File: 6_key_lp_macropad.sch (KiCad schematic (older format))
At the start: 15 parts, among them SW1 Rotary_Encoder_Switch, SW2 SW_Push, U1 ProMicro

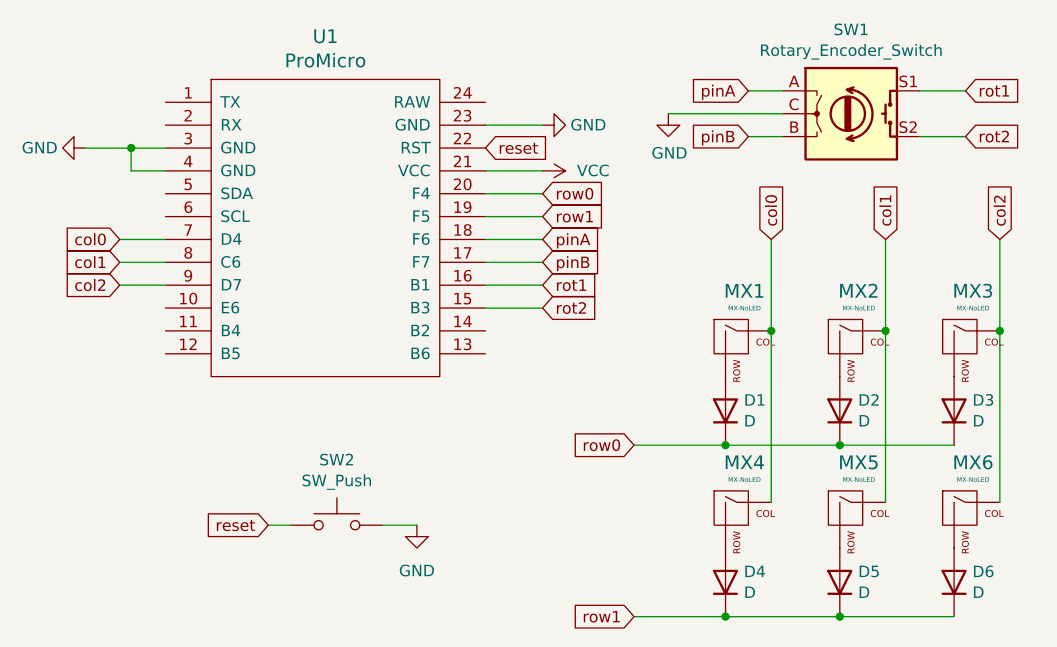
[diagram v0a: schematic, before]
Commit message: Changed to Direct Pin assignment
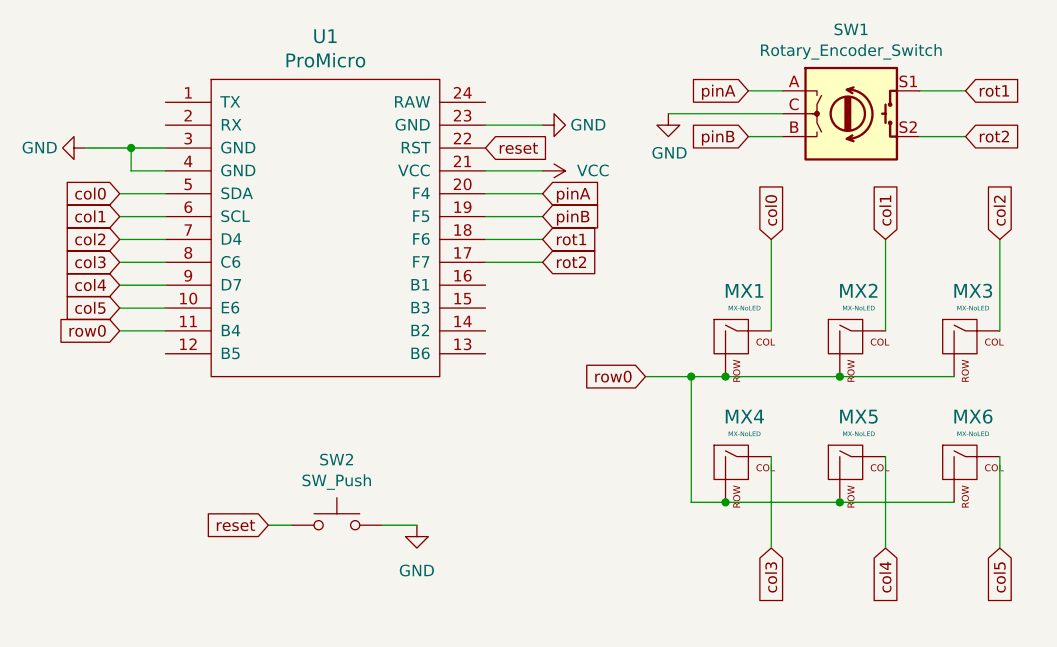
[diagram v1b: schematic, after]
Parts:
- removed D1, D2, D3, D4, D5, D6: D, symbol Device:D
- MX1, MX2, MX3, MX4, MX5, MX6: footprint (none) -> Kailh_Choc:KailhChoc-1U
- SW1: footprint (none) -> Rotary_Encoder:RotaryEncoder_Alps_EC11E-Switch_Vertical_H20mm
- SW2: footprint (none) -> random-keyboard-parts:SKQG-1155865
- U1: footprint (none) -> promicro:ProMicro
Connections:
- net row1 is gone; now on net pinB: U1.19 (F5)
- net col0: now also U1.5 (SDA); no longer MX4.1 (COL), U1.7 (D4)
- net col1: now also U1.6 (SCL); no longer MX5.1 (COL), U1.8 (C6)
- net col2: now also U1.7 (D4); no longer MX6.1 (COL), U1.9 (D7)
- net pinA: now also U1.20 (F4); no longer U1.18 (F6)
- net pinB: no longer U1.17 (F7)
- net rot1: now also U1.18 (F6); no longer U1.16 (B1)
- net rot2: now also U1.17 (F7); no longer U1.15 (B3)
- net row0: now also MX1.2 (ROW), MX2.2 (ROW), MX3.2 (ROW), MX4.2 (ROW), MX5.2 (ROW), MX6.2 (ROW), U1.11 (B4); no longer U1.20 (F4)
- net col5: now reaches U1.10 (E6)
- net col5: now also MX6.1 (COL)
- new net col3: MX4.1 (COL), U1.8 (C6)
- new net col4: MX5.1 (COL), U1.9 (D7)
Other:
- moved on the sheet: MX4, MX5, MX6
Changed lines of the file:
@@
 F 0 "U1" H 4900 4787 60  0000 C CNN
 F 1 "ProMicro" H 4900 4681 60  0000 C CNN
-F 2 "" H 5000 2700 60  0000 C CNN
+F 2 "promicro:ProMicro" H 5000 2700 60  0001 C CNN
 F 3 "" H 5000 2700 60  0000 C CNN
 	1    4900 3750
@@
 F 0 "SW1" H 7200 3417 50  0000 C CNN
 F 1 "Rotary_Encoder_Switch" H 7200 3326 50  0000 C CNN
-F 2 "" H 7050 3210 50  0001 C CNN
+F 2 "Rotary_Encoder:RotaryEncoder_Alps_EC11E-Switch_Vertical_H20mm" H 7050 3210 50  0001 C CNN
 F 3 "~" H 7200 3310 50  0001 C CNN
 	1    7200 3050
@@
 Wire Wire Line
 	5600 3300 5850 3300
+Text GLabel 4000 3400 0    50   Input ~ 0
+col0
+Wire Wire Line
+	4200 3400 4000 3400
+Text GLabel 4000 3500 0    50   Input ~ 0
+col1
+Wire Wire Line
+	4200 3500 4000 3500
 Text GLabel 4000 3600 0    50   Input ~ 0
-col0
+col2
 Wire Wire Line
 	4200 3600 4000 3600
-Text GLabel 4000 3700 0    50   Input ~ 0
-col1
-Wire Wire Line
-	4200 3700 4000 3700
-Text GLabel 4000 3800 0    50   Input ~ 0
-col2
-Wire Wire Line
-	4200 3800 4000 3800
 $Comp
 L power:GND #PWR0104
@@
 F 0 "MX1" H 6733 4273 60  0000 C CNN
 F 1 "MX-NoLED" H 6733 4199 20  0000 C CNN
-F 2 "" H 6075 4025 60  0001 C CNN
+F 2 "Kailh_Choc:KailhChoc-1U" H 6075 4025 60  0001 C CNN
 F 3 "" H 6075 4025 60  0001 C CNN
 	1    6700 4050
@@
 F 0 "MX2" H 7233 4273 60  0000 C CNN
 F 1 "MX-NoLED" H 7233 4199 20  0000 C CNN
-F 2 "" H 6575 4025 60  0001 C CNN
+F 2 "Kailh_Choc:KailhChoc-1U" H 6575 4025 60  0001 C CNN
 F 3 "" H 6575 4025 60  0001 C CNN
 	1    7200 4050
@@
 F 0 "MX3" H 7733 4273 60  0000 C CNN
 F 1 "MX-NoLED" H 7733 4199 20  0000 C CNN
-F 2 "" H 7075 4025 60  0001 C CNN
+F 2 "Kailh_Choc:KailhChoc-1U" H 7075 4025 60  0001 C CNN
 F 3 "" H 7075 4025 60  0001 C CNN
 	1    7700 4050
@@
 L MX_Alps_Hybrid:MX-NoLED MX6
 U 1 1 62CCE05A
-P 7700 4800
-F 0 "MX6" H 7733 5023 60  0000 C CNN
-F 1 "MX-NoLED" H 7733 4949 20  0000 C CNN
-F 2 "" H 7075 4775 60  0001 C CNN
-F 3 "" H 7075 4775 60  0001 C CNN
-	1    7700 4800
+P 7700 4600
+F 0 "MX6" H 7733 4823 60  0000 C CNN
+F 1 "MX-NoLED" H 7733 4749 20  0000 C CNN
+F 2 "Kailh_Choc:KailhChoc-1U" H 7075 4575 60  0001 C CNN
+F 3 "" H 7075 4575 60  0001 C CNN
+	1    7700 4600
 	1    0    0    -1
 $EndComp
@@
 L MX_Alps_Hybrid:MX-NoLED MX5
 U 1 1 62CCE444
-P 7200 4800
-F 0 "MX5" H 7233 5023 60  0000 C CNN
-F 1 "MX-NoLED" H 7233 4949 20  0000 C CNN
-F 2 "" H 6575 4775 60  0001 C CNN
-F 3 "" H 6575 4775 60  0001 C CNN
-	1    7200 4800
+P 7200 4600
+F 0 "MX5" H 7233 4823 60  0000 C CNN
+F 1 "MX-NoLED" H 7233 4749 20  0000 C CNN
+F 2 "Kailh_Choc:KailhChoc-1U" H 6575 4575 60  0001 C CNN
+F 3 "" H 6575 4575 60  0001 C CNN
+	1    7200 4600
 	1    0    0    -1
 $EndComp
@@
 L MX_Alps_Hybrid:MX-NoLED MX4
 U 1 1 62CCEA2C
-P 6700 4800
-F 0 "MX4" H 6733 5023 60  0000 C CNN
-F 1 "MX-NoLED" H 6733 4949 20  0000 C CNN
-F 2 "" H 6075 4775 60  0001 C CNN
-F 3 "" H 6075 4775 60  0001 C CNN
-	1    6700 4800
-	1    0    0    -1
-$EndComp
-Text GLabel 5850 3900 2    50   Input ~ 0
+P 6700 4600
+F 0 "MX4" H 6733 4823 60  0000 C CNN
+F 1 "MX-NoLED" H 6733 4749 20  0000 C CNN
+F 2 "Kailh_Choc:KailhChoc-1U" H 6075 4575 60  0001 C CNN
+F 3 "" H 6075 4575 60  0001 C CNN
+	1    6700 4600
+	1    0    0    -1
+$EndComp
+Text GLabel 5850 3700 2    50   Input ~ 0
 rot2
-Text GLabel 5850 3800 2    50   Input ~ 0
+Text GLabel 5850 3600 2    50   Input ~ 0
 rot1
-Text GLabel 5850 3700 2    50   Input ~ 0
+Text GLabel 5850 3500 2    50   Input ~ 0
 pinB
-Text GLabel 5850 3600 2    50   Input ~ 0
+Text GLabel 5850 3400 2    50   Input ~ 0
 pinA
-Text GLabel 5850 3500 2    50   Input ~ 0
-row1
-Text GLabel 5850 3400 2    50   Input ~ 0
+Text GLabel 4000 4000 0    50   Input ~ 0
 row0
 Wire Wire Line
@@
 Wire Wire Line
 	5600 3700 5850 3700
-Wire Wire Line
-	5600 3800 5850 3800
-Wire Wire Line
-	5600 3900 5850 3900
 Text GLabel 7700 2950 2    50   Input ~ 0
 rot1
@@
 Wire Wire Line
 	7850 3600 7850 4000
-Text GLabel 6250 4500 0    50   Input ~ 0
+Text GLabel 6300 4200 0    50   Input ~ 0
 row0
-Text GLabel 6250 5250 0    50   Input ~ 0
-row1
-Wire Wire Line
-	7850 4000 7850 4750
-Wire Wire Line
-	7350 4000 7350 4750
-Wire Wire Line
-	6850 4000 6850 4750
-$Comp
-L Device:D D1
-U 1 1 62CE7421
-P 6650 4350
-F 0 "D1" V 6696 4270 50  0000 R CNN
-F 1 "D" V 6605 4270 50  0000 R CNN
-F 2 "" H 6650 4350 50  0001 C CNN
-F 3 "~" H 6650 4350 50  0001 C CNN
-	1    6650 4350
-	0    -1   -1   0
-$EndComp
-$Comp
-L Device:D D2
-U 1 1 62CEBAD1
-P 7150 4350
-F 0 "D2" V 7196 4270 50  0000 R CNN
-F 1 "D" V 7105 4270 50  0000 R CNN
-F 2 "" H 7150 4350 50  0001 C CNN
-F 3 "~" H 7150 4350 50  0001 C CNN
-	1    7150 4350
-	0    -1   -1   0
-$EndComp
-$Comp
-L Device:D D3
-U 1 1 62CEBF48
-P 7650 4350
-F 0 "D3" V 7696 4270 50  0000 R CNN
-F 1 "D" V 7605 4270 50  0000 R CNN
-F 2 "" H 7650 4350 50  0001 C CNN
-F 3 "~" H 7650 4350 50  0001 C CNN
-	1    7650 4350
-	0    -1   -1   0
-$EndComp
-Wire Wire Line
-	6650 4500 7150 4500
-Connection ~ 7150 4500
-Wire Wire Line
-	7150 4500 7650 4500
-Connection ~ 6850 4000
-Connection ~ 7350 4000
-Connection ~ 7850 4000
-$Comp
-L Device:D D4
-U 1 1 62CEFF8A
-P 6650 5100
-F 0 "D4" V 6696 5020 50  0000 R CNN
-F 1 "D" V 6605 5020 50  0000 R CNN
-F 2 "" H 6650 5100 50  0001 C CNN
-F 3 "~" H 6650 5100 50  0001 C CNN
-	1    6650 5100
-	0    -1   -1   0
-$EndComp
-$Comp
-L Device:D D5
-U 1 1 62CF0730
-P 7150 5100
-F 0 "D5" V 7196 5020 50  0000 R CNN
-F 1 "D" V 7105 5020 50  0000 R CNN
-F 2 "" H 7150 5100 50  0001 C CNN
-F 3 "~" H 7150 5100 50  0001 C CNN
-	1    7150 5100
-	0    -1   -1   0
-$EndComp
-$Comp
-L Device:D D6
-U 1 1 62CF0D5A
-P 7650 5100
-F 0 "D6" V 7696 5020 50  0000 R CNN
-F 1 "D" V 7605 5020 50  0000 R CNN
-F 2 "" H 7650 5100 50  0001 C CNN
-F 3 "~" H 7650 5100 50  0001 C CNN
-	1    7650 5100
-	0    -1   -1   0
-$EndComp
-Wire Wire Line
-	6650 5250 7150 5250
-Connection ~ 7150 5250
-Wire Wire Line
-	7150 5250 7650 5250
-Wire Wire Line
-	6650 4500 6250 4500
-Connection ~ 6650 4500
-Wire Wire Line
-	6650 5250 6250 5250
-Connection ~ 6650 5250
 Text GLabel 4650 4850 0    50   Input ~ 0
 reset
@@
 F 0 "SW2" H 4950 5135 50  0000 C CNN
 F 1 "SW_Push" H 4950 5044 50  0000 C CNN
-F 2 "" H 4950 5050 50  0001 C CNN
+F 2 "random-keyboard-parts:SKQG-1155865" H 4950 5050 50  0001 C CNN
 F 3 "~" H 4950 5050 50  0001 C CNN
 	1    4950 4850
@@
 Wire Wire Line
 	4650 4850 4750 4850
+Text GLabel 4000 3700 0    50   Input ~ 0
+col3
+Text GLabel 4000 3800 0    50   Input ~ 0
+col4
+Text GLabel 4000 3900 0    50   Input ~ 0
+col5
+Wire Wire Line
+	6300 4200 6500 4200
+Connection ~ 6650 4200
+Wire Wire Line
+	6650 4200 7150 4200
+Connection ~ 7150 4200
+Wire Wire Line
+	7150 4200 7650 4200
+Wire Wire Line
+	6500 4200 6500 4750
+Wire Wire Line
+	6500 4750 6650 4750
+Connection ~ 6500 4200
+Wire Wire Line
+	6500 4200 6650 4200
+Connection ~ 6650 4750
+Wire Wire Line
+	6650 4750 7150 4750
+Connection ~ 7150 4750
+Wire Wire Line
+	7150 4750 7650 4750
+Text GLabel 7350 4950 3    50   Input ~ 0
+col4
+Text GLabel 7850 4950 3    50   Input ~ 0
+col5
+Text GLabel 6850 4950 3    50   Input ~ 0
+col3
+Wire Wire Line
+	4000 3700 4200 3700
+Wire Wire Line
+	4200 3800 4000 3800
+Wire Wire Line
+	4200 3900 4000 3900
+Wire Wire Line
+	4000 4000 4200 4000
+Wire Wire Line
+	7850 4950 7850 4550
+Wire Wire Line
+	7350 4950 7350 4550
+Wire Wire Line
+	6850 4950 6850 4550
 $EndSCHEMATC

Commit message: Made the first PCB version
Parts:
- U1: footprint promicro:ProMicro -> promicro:ProMicro-NoSilk
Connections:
- net col0: now also U1.6 (SCL); no longer U1.5 (SDA)
- net col1: now also U1.7 (D4); no longer U1.6 (SCL)
- net col2: now also U1.9 (D7); no longer U1.7 (D4)
- net col4: now also U1.11 (B4); no longer U1.9 (D7)
- net pinA: now also U1.19 (F5); no longer U1.20 (F4)
- net pinB: now also U1.20 (F4); no longer U1.19 (F5)
- net row0: now also U1.5 (SDA); no longer U1.11 (B4)
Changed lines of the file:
@@
 F 0 "U1" H 4900 4787 60  0000 C CNN
 F 1 "ProMicro" H 4900 4681 60  0000 C CNN
-F 2 "promicro:ProMicro" H 5000 2700 60  0001 C CNN
+F 2 "promicro:ProMicro-NoSilk" H 5000 2700 60  0001 C CNN
 F 3 "" H 5000 2700 60  0000 C CNN
 	1    4900 3750
@@
 Wire Wire Line
 	5600 3300 5850 3300
-Text GLabel 4000 3400 0    50   Input ~ 0
-col0
 Wire Wire Line
 	4200 3400 4000 3400
-Text GLabel 4000 3500 0    50   Input ~ 0
-col1
 Wire Wire Line
 	4200 3500 4000 3500
-Text GLabel 4000 3600 0    50   Input ~ 0
-col2
 Wire Wire Line
 	4200 3600 4000 3600
@@
 Text GLabel 5850 3600 2    50   Input ~ 0
 rot1
+Text GLabel 5850 3400 2    50   Input ~ 0
+pinB
 Text GLabel 5850 3500 2    50   Input ~ 0
-pinB
-Text GLabel 5850 3400 2    50   Input ~ 0
 pinA
-Text GLabel 4000 4000 0    50   Input ~ 0
-row0
 Wire Wire Line
 	5600 3400 5850 3400
@@
 Wire Wire Line
 	4650 4850 4750 4850
-Text GLabel 4000 3700 0    50   Input ~ 0
-col3
-Text GLabel 4000 3800 0    50   Input ~ 0
+Text GLabel 4000 4000 0    50   Input ~ 0
 col4
 Text GLabel 4000 3900 0    50   Input ~ 0
@@
 Wire Wire Line
 	6850 4950 6850 4550
+Text GLabel 4000 3400 0    50   Input ~ 0
+row0
+Text GLabel 4000 3700 0    50   Input ~ 0
+col3
+Text GLabel 4000 3800 0    50   Input ~ 0
+col2
+Text GLabel 4000 3600 0    50   Input ~ 0
+col1
+Text GLabel 4000 3500 0    50   Input ~ 0
+col0
 $EndSCHEMATC

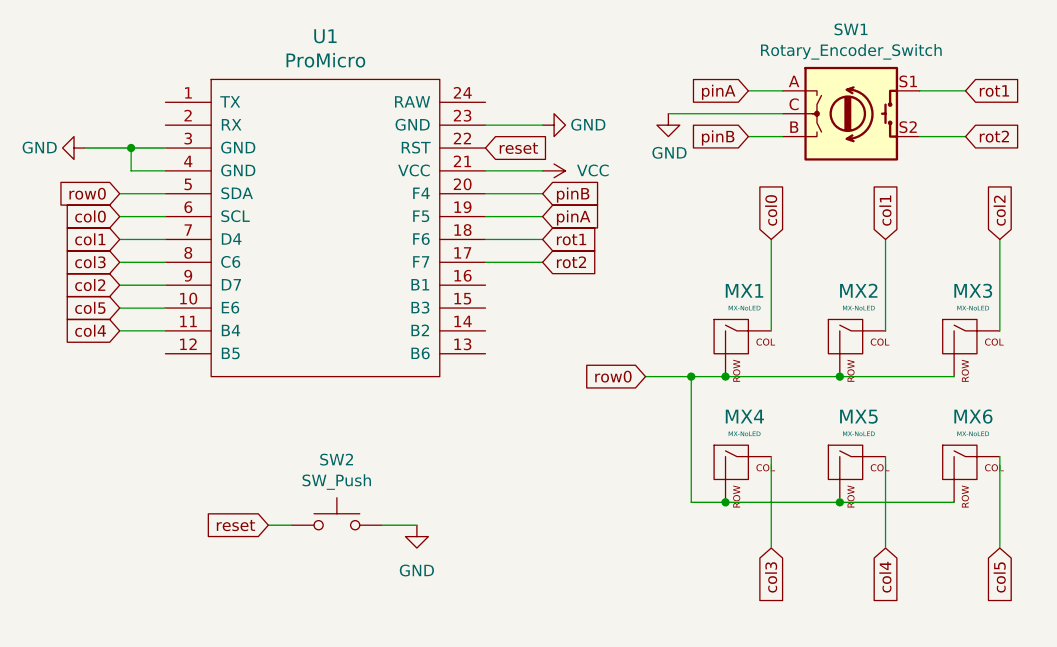
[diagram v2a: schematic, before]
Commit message: Flipped MCU to allow for stronger USB connector
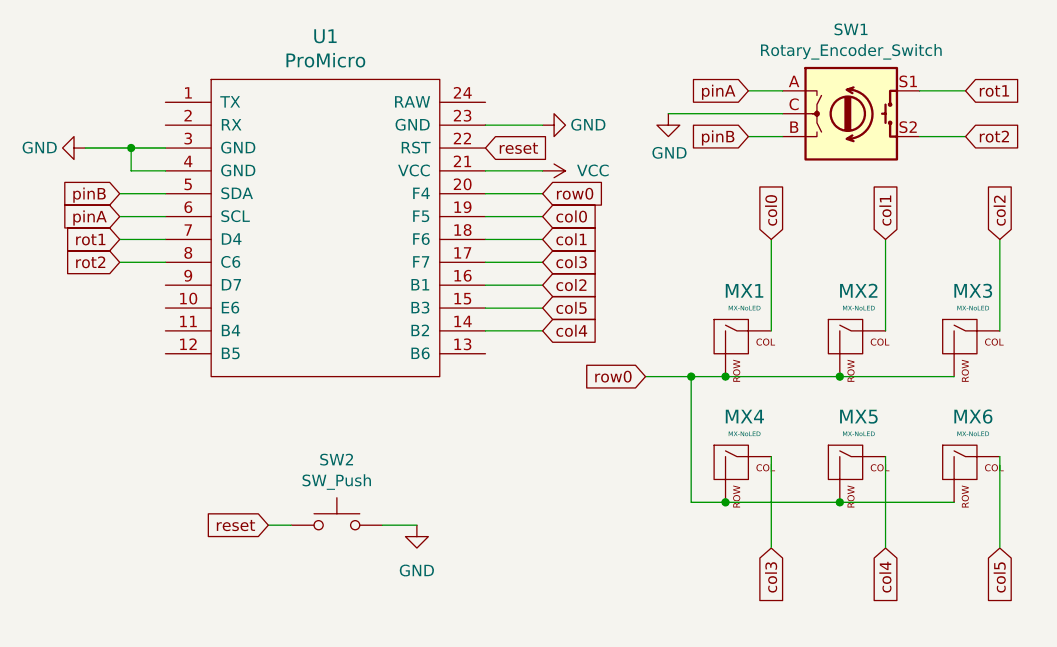
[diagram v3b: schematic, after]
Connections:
- net col0: now also U1.19 (F5); no longer U1.6 (SCL)
- net col1: now also U1.18 (F6); no longer U1.7 (D4)
- net col2: now also U1.16 (B1); no longer U1.9 (D7)
- net col3: now also U1.17 (F7); no longer U1.8 (C6)
- net col4: now also U1.14 (B2); no longer U1.11 (B4)
- net col5: now also U1.15 (B3); no longer U1.10 (E6)
- net pinA: now also U1.6 (SCL); no longer U1.19 (F5)
- net pinB: now also U1.5 (SDA); no longer U1.20 (F4)
- net rot1: now also U1.7 (D4); no longer U1.18 (F6)
- net rot2: now also U1.8 (C6); no longer U1.17 (F7)
- net row0: now also U1.20 (F4); no longer U1.5 (SDA)
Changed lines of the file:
@@
 	1    0    0    -1
 $EndComp
-Text GLabel 5850 3700 2    50   Input ~ 0
+Text GLabel 4000 3700 0    50   Input ~ 0
 rot2
-Text GLabel 5850 3600 2    50   Input ~ 0
-rot1
-Text GLabel 5850 3400 2    50   Input ~ 0
+Text GLabel 4000 3400 0    50   Input ~ 0
 pinB
-Text GLabel 5850 3500 2    50   Input ~ 0
+Text GLabel 4000 3500 0    50   Input ~ 0
 pinA
 Wire Wire Line
@@
 Wire Wire Line
 	4650 4850 4750 4850
-Text GLabel 4000 4000 0    50   Input ~ 0
+Text GLabel 5850 4000 2    50   Input ~ 0
 col4
-Text GLabel 4000 3900 0    50   Input ~ 0
+Text GLabel 5850 3900 2    50   Input ~ 0
 col5
 Wire Wire Line
@@
 	4000 3700 4200 3700
 Wire Wire Line
-	4200 3800 4000 3800
-Wire Wire Line
-	4200 3900 4000 3900
-Wire Wire Line
-	4000 4000 4200 4000
-Wire Wire Line
 	7850 4950 7850 4550
 Wire Wire Line
@@
 Wire Wire Line
 	6850 4950 6850 4550
-Text GLabel 4000 3400 0    50   Input ~ 0
+Text GLabel 5850 3400 2    50   Input ~ 0
 row0
-Text GLabel 4000 3700 0    50   Input ~ 0
+Text GLabel 5850 3700 2    50   Input ~ 0
 col3
-Text GLabel 4000 3800 0    50   Input ~ 0
+Text GLabel 5850 3800 2    50   Input ~ 0
 col2
+Text GLabel 5850 3600 2    50   Input ~ 0
+col1
+Text GLabel 5850 3500 2    50   Input ~ 0
+col0
 Text GLabel 4000 3600 0    50   Input ~ 0
-col1
-Text GLabel 4000 3500 0    50   Input ~ 0
-col0
+rot1
+Wire Wire Line
+	5600 3800 5850 3800
+Wire Wire Line
+	5600 3900 5850 3900
+Wire Wire Line
+	5600 4000 5850 4000
 $EndSCHEMATC

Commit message: Corrected for direct pin assignment
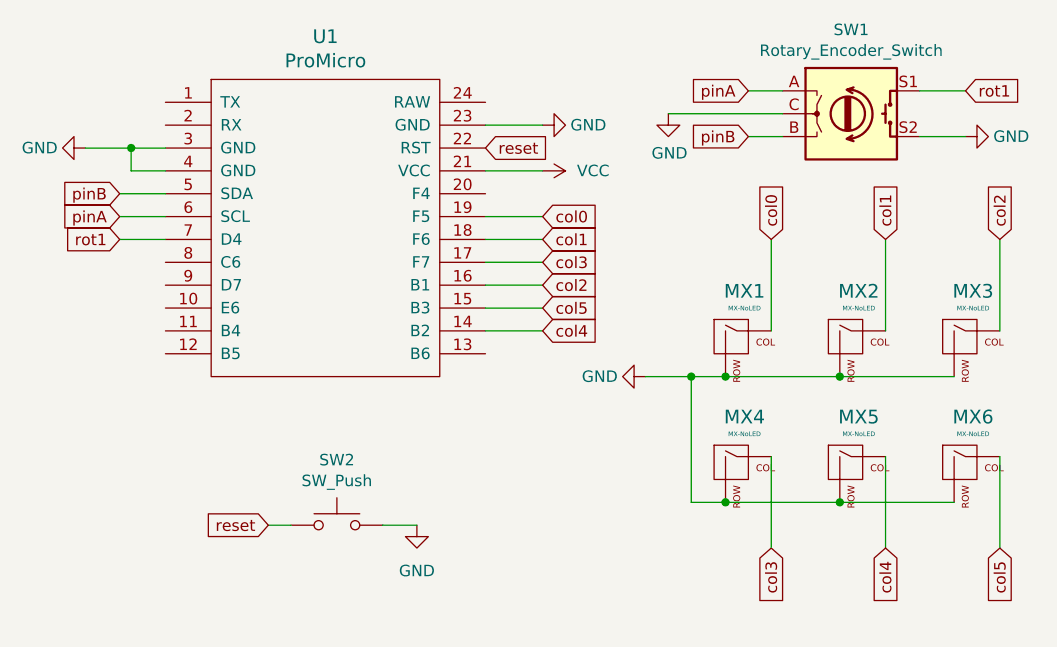
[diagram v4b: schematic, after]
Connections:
- net GND: now also MX1.2 (ROW), MX2.2 (ROW), MX3.2 (ROW), MX4.2 (ROW), MX5.2 (ROW), MX6.2 (ROW), SW1.S2
- net rot2: no longer names the net of U1.8 (C6)
- net rot2: no longer SW1.S2
- removed net row0: MX1.2 (ROW), MX2.2 (ROW), MX3.2 (ROW), MX4.2 (ROW), MX5.2 (ROW), MX6.2 (ROW), U1.20 (F4)
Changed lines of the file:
@@
 	1    0    0    -1
 $EndComp
-Text GLabel 4000 3700 0    50   Input ~ 0
-rot2
 Text GLabel 4000 3400 0    50   Input ~ 0
 pinB
 Text GLabel 4000 3500 0    50   Input ~ 0
 pinA
-Wire Wire Line
-	5600 3400 5850 3400
 Wire Wire Line
 	5600 3500 5850 3500
@@
 Text GLabel 7700 2950 2    50   Input ~ 0
 rot1
-Text GLabel 7700 3150 2    50   Input ~ 0
-rot2
 Wire Wire Line
 	7500 2950 7700 2950
@@
 Wire Wire Line
 	7850 3600 7850 4000
-Text GLabel 6300 4200 0    50   Input ~ 0
-row0
 Text GLabel 4650 4850 0    50   Input ~ 0
 reset
@@
 col3
 Wire Wire Line
-	4000 3700 4200 3700
-Wire Wire Line
 	7850 4950 7850 4550
 Wire Wire Line
@@
 Wire Wire Line
 	6850 4950 6850 4550
-Text GLabel 5850 3400 2    50   Input ~ 0
-row0
 Text GLabel 5850 3700 2    50   Input ~ 0
 col3
@@
 Wire Wire Line
 	5600 4000 5850 4000
+$Comp
+L power:GND #PWR?
+U 1 1 62CE2DDB
+P 6300 4200
+F 0 "#PWR?" H 6300 3950 50  0001 C CNN
+F 1 "GND" V 6300 4000 50  0000 C CNN
+F 2 "" H 6300 4200 50  0001 C CNN
+F 3 "" H 6300 4200 50  0001 C CNN
+	1    6300 4200
+	0    1    1    0
+$EndComp
+$Comp
+L power:GND #PWR?
+U 1 1 62CE4351
+P 7700 3150
+F 0 "#PWR?" H 7700 2900 50  0001 C CNN
+F 1 "GND" V 7700 2950 50  0000 C CNN
+F 2 "" H 7700 3150 50  0001 C CNN
+F 3 "" H 7700 3150 50  0001 C CNN
+	1    7700 3150
+	0    -1   -1   0
+$EndComp
 $EndSCHEMATC
